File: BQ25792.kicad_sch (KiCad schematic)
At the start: 32 parts, among them U1 BQ25792

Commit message: More fixes
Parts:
- TH1: FT Rotation Offset (none) -> 180
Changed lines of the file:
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@@
+			)
+		)
+		(property "FT Rotation Offset" "180"
+			(at 162.56 100.33 0)
+			(effects
+				(font
+					(size 1.27 1.27)
+				)
+				(hide yes)
 			)
 		)

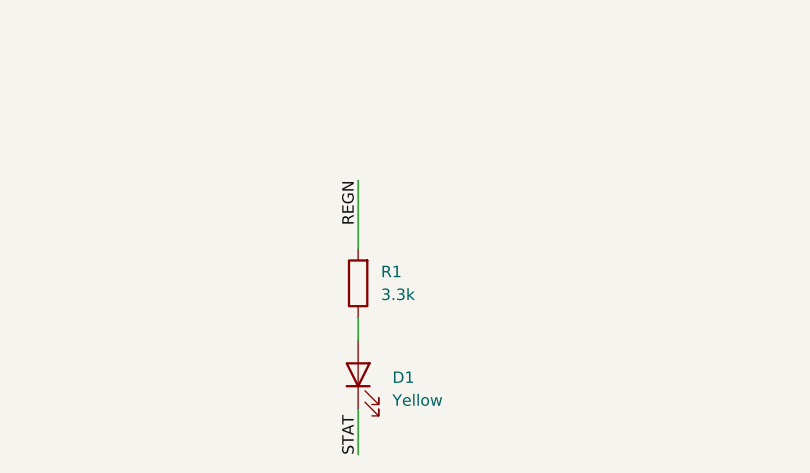
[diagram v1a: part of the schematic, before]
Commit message: Set LED resistors
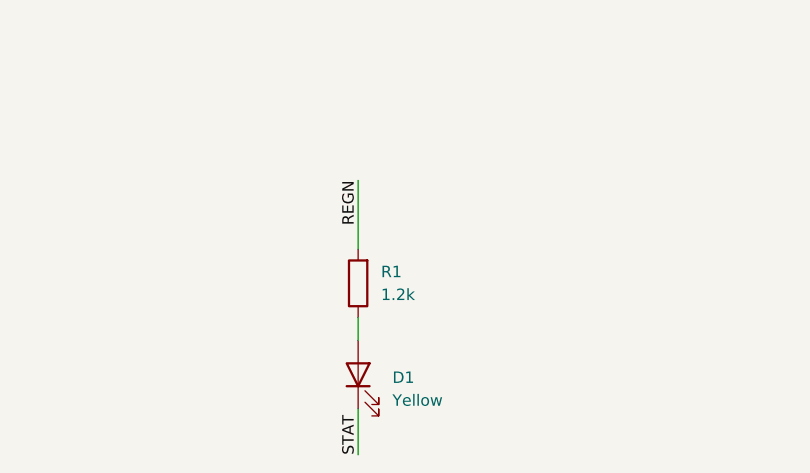
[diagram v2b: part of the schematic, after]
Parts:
- R1: value 3.3k -> 1.2k
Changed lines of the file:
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@@
 		(fields_autoplaced yes)
 		(property "Reference" "R1"
-			(at 125.73 153.67 0)
+			(at 125.73 153.6699 0)
 			(effects
 				(font
@@
 			)
 		)
-		(property "Value" "3.3k"
-			(at 125.73 156.21 0)
+		(property "Value" "1.2k"
+			(at 125.73 156.2099 0)
 			(effects
 				(font

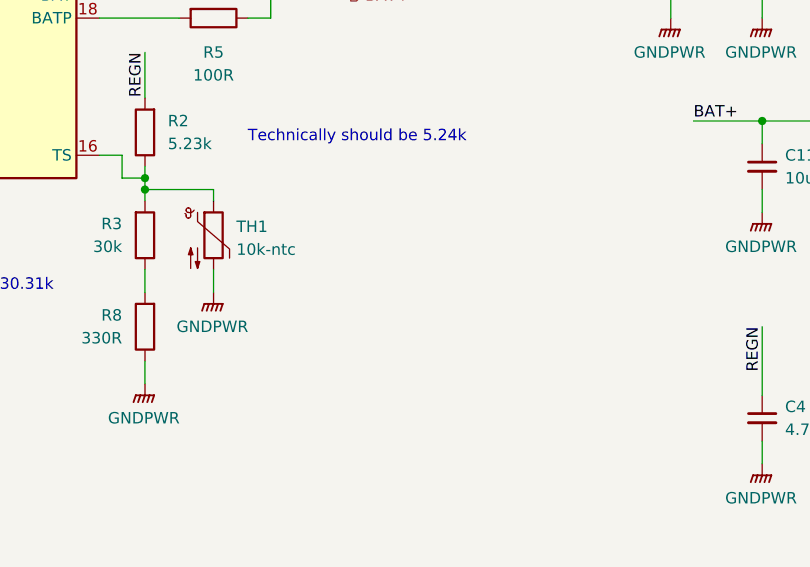
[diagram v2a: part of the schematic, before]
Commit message: Switch to JST-PH connectors Add Sheet titles
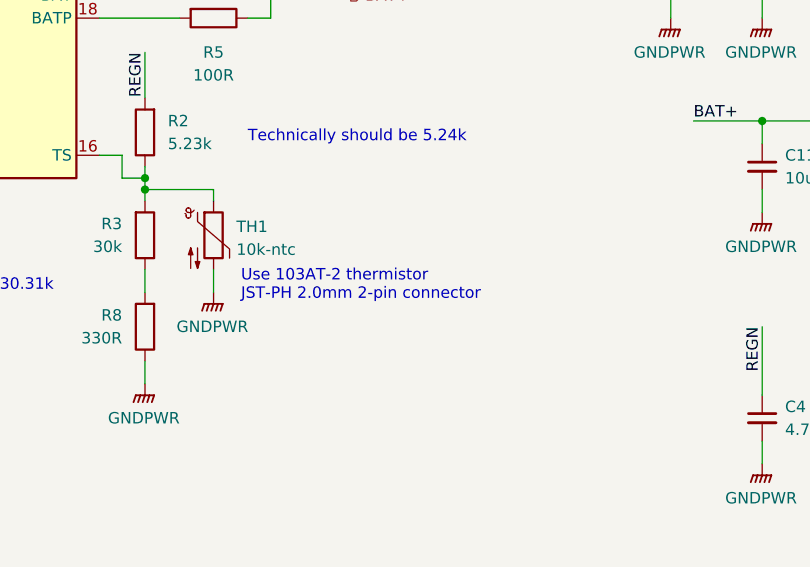
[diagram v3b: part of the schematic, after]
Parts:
- TH1: footprint Connector_JST:JST_ZH_B2B-ZR_1x02_P1.50mm_Vertical -> Connector_JST:JST_PH_B2B-PH-K_1x02_P2.00mm_Vertical
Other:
- note added: "Use 103AT-2 thermistor JST-PH 2.0mm 2-pin connector"
- title: (none) -> BQ25792 Buck-Boost Charger
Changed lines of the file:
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@@
 	(paper "A4")
 	(title_block
+		(title "BQ25792 Buck-Boost Charger")
 		(rev "1.0")
+		(comment 1 "Through-hole connectors not to be installed as part of PCBA")
+		(comment 2 "5-22V input 5A max, 1A max without MCU control")
 	)
 	(text "2.25A Initial limit,\noverrideable from I2C"
@@
 			)
 			(justify left bottom)
+		)
+	)
+	(text "Use 103AT-2 thermistor\nJST-PH 2.0mm 2-pin connector"
+		(exclude_from_sim no)
+		(at 165.608 105.918 0)
+		(effects
+			(font
+				(size 1.27 1.27)
+			)
+			(justify left)
 		)
 	)
@@
 			)
 		)
-		(property "Footprint" "Connector_JST:JST_ZH_B2B-ZR_1x02_P1.50mm_Vertical"
+		(property "Footprint" "Connector_JST:JST_PH_B2B-PH-K_1x02_P2.00mm_Vertical"
 			(at 162.56 99.06 0)
 			(effects

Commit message: Action review feedback
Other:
- note added: "Charge current defaults to 1A at startup. Over I2C this can be raised to 5A."
- note added: "UVLO is fixed @ 3.6V"
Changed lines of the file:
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@@
 		(comment 2 "5-22V input 5A max, 1A max without MCU control")
+	)
+	(text "UVLO is fixed @ 3.6V"
+		(exclude_from_sim no)
+		(at 42.164 39.37 0)
+		(effects
+			(font
+				(size 1.27 1.27)
+			)
+		)
 	)
 	(text "2.25A Initial limit,\noverrideable from I2C"
@@
 		)
 	)
+	(text "Charge current defaults to 1A at startup.\nOver I2C this can be raised to 5A."
+		(exclude_from_sim no)
+		(at 82.042 35.052 0)
+		(effects
+			(font
+				(size 1.27 1.27)
+			)
+		)
+	)
